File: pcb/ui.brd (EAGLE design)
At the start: 90 x 15 mm, 18 parts, among them IC1 SN74LVC14APW, X1 MOLEX_1MM_FPC, X2 PVA2OAH11.7NV2, X3 PVA2OAH11.7NV2, X4 PVA2OAH11.7NV2, X5 PVA2OAH11.7NV2

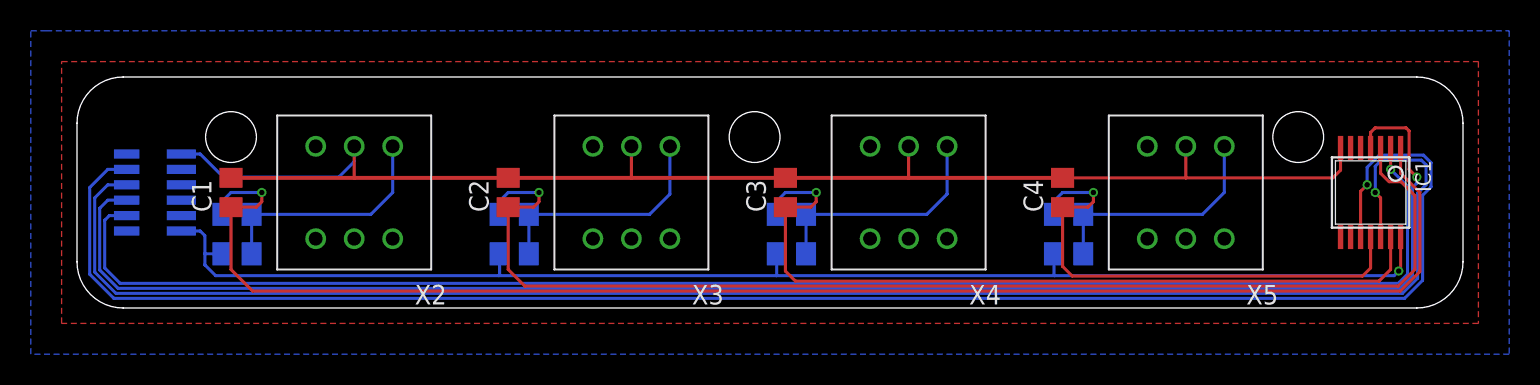
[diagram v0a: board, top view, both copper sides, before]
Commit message: Board dimension created
-reworked schematics
-added PCB for battery-holder
-added PCB for UI
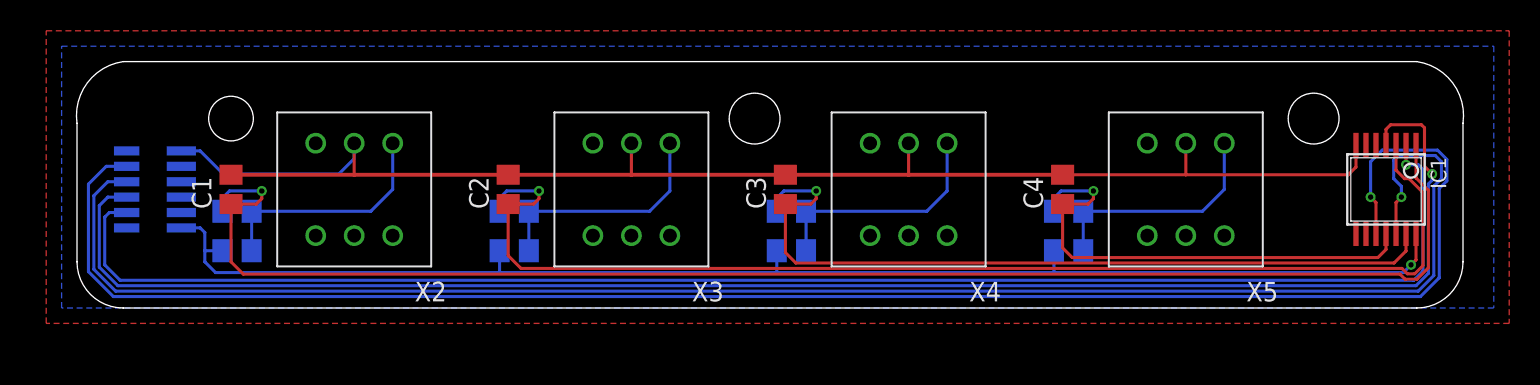
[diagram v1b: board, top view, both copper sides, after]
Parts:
- moved IC1 1.02 mm to (85.0, 7.70)
- moved C1 0.20 mm to (10.0, 7.70)
- moved C2 0.20 mm to (28.0, 7.70)
- moved C3 0.20 mm to (46.0, 7.70)
- moved C4 0.20 mm to (64.0, 7.70)
- moved R1 0.20 mm to (10.4, 3.72)
- moved R2 0.20 mm to (10.4, 6.28)
- moved R3 0.20 mm to (28.4, 3.72)
- moved R4 0.20 mm to (28.4, 6.28)
- moved R5 0.20 mm to (46.4, 3.72)
- moved R6 0.20 mm to (46.4, 6.28)
- moved R7 0.20 mm to (64.4, 3.72)
- moved R8 0.20 mm to (64.4, 6.28)
- moved X1 0.20 mm to (5.00, 7.70)
- moved X2 0.20 mm to (18.0, 7.70)
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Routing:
- net UI_BUTTON_INT_3: track 113.4 -> 115.8 mm
- net UI_BUTTON_INT_0: track 98.5 -> 100.0 mm
- net UI_BUTTON_INT_2: track 110.0 -> 111.4 mm
- net N$13: track 32.7 -> 31.6 mm
- net N$11: track 52.6 -> 51.4 mm
- net UI_BUTTON_INT_1: track 105.5 -> 106.6 mm
- net N$9: track 79.5 -> 78.4 mm
- net GND: track 95.1 -> 96.1 mm
- net +3V3: track 89.2 -> 90.0 mm
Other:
- board size 90 x 15 mm -> 90.1 x 16 mm
